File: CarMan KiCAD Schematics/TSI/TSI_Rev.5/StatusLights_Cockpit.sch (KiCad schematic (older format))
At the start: 16 parts, among them U1 RDE03110S12, U11 TLP293, U13 TLP293

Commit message: Datasheets and notes
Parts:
- D1: value Green LED -> GREEN LED; Part Name (none) -> VAOL-S8GT4
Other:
- note added: "Brake Light & RTDS\n(J18)\n"
- note added: "COCKPIT\n(J8)\n"
- note removed: "J8 COCKPIT\n"
- moved on the sheet: R15, R99, U11
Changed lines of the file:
@@
 L TSI_Rev.5-rescue:TLP293-CarMan_KiCAD_Library-TSI_Rev.5-rescue U11
 U 1 1 5F9A966C
-P 9175 3700
-F 0 "U11" H 9175 3900 50  0000 C CNN
-F 1 "TLP293" H 9175 3500 50  0000 C CNN
-F 2 "Package_SO:SOIC-4_4.55x2.6mm_P1.27mm" H 8975 3500 50  0001 L CIN
-F 3 "" H 9175 3700 50  0001 L CNN
-	1    9175 3700
+P 8875 3550
+F 0 "U11" H 8875 3750 50  0000 C CNN
+F 1 "TLP293" H 8875 3350 50  0000 C CNN
+F 2 "Package_SO:SOIC-4_4.55x2.6mm_P1.27mm" H 8675 3350 50  0001 L CIN
+F 3 "https://www.mouser.com/datasheet/2/408/Toshiba_TLP293_datasheet-1209449.pdf" H 8875 3550 50  0001 L CNN
+	1    8875 3550
 	1    0    0    -1
 $EndComp
@@
 L Device:R R15
 U 1 1 5F9DEF51
-P 8525 3600
-F 0 "R15" V 8425 3600 50  0000 C CNN
-F 1 "300" V 8525 3600 50  0000 C CNN
-F 2 "Resistor_SMD:R_0805_2012Metric_Pad1.15x1.40mm_HandSolder" V 8455 3600 50  0001 C CNN
-F 3 "~" H 8525 3600 50  0001 C CNN
-	1    8525 3600
+P 8225 3450
+F 0 "R15" V 8125 3450 50  0000 C CNN
+F 1 "300" V 8225 3450 50  0000 C CNN
+F 2 "Resistor_SMD:R_0805_2012Metric_Pad1.15x1.40mm_HandSolder" V 8155 3450 50  0001 C CNN
+F 3 "~" H 8225 3450 50  0001 C CNN
+	1    8225 3450
 	0    1    1    0
 $EndComp
-Text Label 10025 3600 2    50   ~ 0
+Text Label 9725 3450 2    50   ~ 0
 24V
-Text Label 10025 3800 2    50   ~ 0
+Text Label 9725 3650 2    50   ~ 0
 Drive_LED
-Text Label 7675 3600 0    50   ~ 0
+Text Label 7375 3450 0    50   ~ 0
 D_LED_CTRL
 Text Label 3875 3900 2    50   ~ 0
@@
 Drive_BTN
 Wire Wire Line
-	8875 3600 8675 3600
+	8575 3450 8375 3450
 Text Notes 7100 6950 0    177  ~ 0
 STATUS LIGHTS, TSAL & RTDS
@@
 F 1 "TLP293" H 2750 4234 50  0000 C CNN
 F 2 "Package_SO:SOIC-4_4.55x2.6mm_P1.27mm" H 2550 3800 50  0001 L CIN
-F 3 "" H 2750 4000 50  0001 L CNN
+F 3 "https://www.mouser.com/datasheet/2/408/Toshiba_TLP293_datasheet-1209449.pdf" H 2750 4000 50  0001 L CNN
 	1    2750 4000
 	1    0    0    -1
@@
 	4400 7000 5000 7000
 Wire Wire Line
-	7675 3600 8375 3600
-Wire Wire Line
-	7675 3800 8875 3800
-Wire Wire Line
-	9475 3600 10025 3600
-Wire Wire Line
-	9475 3800 9550 3800
+	7375 3450 8075 3450
+Wire Wire Line
+	7375 3650 8575 3650
+Wire Wire Line
+	9175 3450 9725 3450
+Wire Wire Line
+	9175 3650 9250 3650
 Wire Notes Line
 	500  2250 2250 2250
@@
 Wire Notes Line
 	500  500  500  2250
-Text Label 7675 3800 0    50   ~ 0
+Text Label 7375 3650 0    50   ~ 0
 5V_ISO_RTN
 $Comp
@@
 Wire Notes Line
 	9350 5850 9350 5500
-Text Notes 9800 5700 2    50   ~ 0
-J8 COCKPIT\n
+Text Notes 9375 5750 0    50   ~ 0
+COCKPIT\n(J8)\n
 Wire Wire Line
 	8600 5350 8900 5350
@@
 L Device:R R?
 U 1 1 605792C2
-P 9550 3950
+P 9250 3800
 AR Path="/5FE1DE7D/605792C2" Ref="R?"  Part="1"
 AR Path="/5FE1DCBA/605792C2" Ref="R99"  Part="1"
-F 0 "R99" V 9450 3950 50  0000 C CNN
-F 1 "1K" V 9550 3950 50  0000 C CNN
-F 2 "Resistor_SMD:R_0805_2012Metric_Pad1.15x1.40mm_HandSolder" V 9480 3950 50  0001 C CNN
-F 3 "~" H 9550 3950 50  0001 C CNN
-	1    9550 3950
-	1    0    0    -1
-$EndComp
-Text Label 9550 4200 0    50   ~ 0
-GLV_RTN
-Wire Wire Line
-	9550 4100 9550 4200
-Connection ~ 9550 3800
-Wire Wire Line
-	9550 3800 10025 3800
+F 0 "R99" V 9150 3800 50  0000 C CNN
+F 1 "1K" V 9250 3800 50  0000 C CNN
+F 2 "Resistor_SMD:R_0805_2012Metric_Pad1.15x1.40mm_HandSolder" V 9180 3800 50  0001 C CNN
+F 3 "~" H 9250 3800 50  0001 C CNN
+	1    9250 3800
+	1    0    0    -1
+$EndComp
+Text Label 9250 4050 0    50   ~ 0
+GLV_RTN
+Wire Wire Line
+	9250 3950 9250 4050
+Connection ~ 9250 3650
+Wire Wire Line
+	9250 3650 9725 3650
 $Comp
 L Device:LED D1
@@
 P 10200 1800
 F 0 "D1" V 10239 1682 50  0000 R CNN
-F 1 "Green LED" V 10148 1682 50  0000 R CNN
+F 1 "GREEN LED" V 10148 1682 50  0000 R CNN
 F 2 "LED_SMD:LED_0805_2012Metric_Pad1.15x1.40mm_HandSolder" H 10200 1800 50  0001 C CNN
-F 3 "~" H 10200 1800 50  0001 C CNN
+F 3 "http://static.vcclite.com/pdf/VAOL-S8GT4-LED-0805-green.pdf" H 10200 1800 50  0001 C CNN
+F 4 "VAOL-S8GT4" V 10200 1800 50  0001 C CNN "Part Name"
 	1    10200 1800
 	0    -1   -1   0
@@
 Wire Wire Line
 	3300 4100 4300 4100
+Text Notes 4225 4375 2    43   ~ 0
+Brake Light & RTDS\n(J18)\n
 $EndSCHEMATC

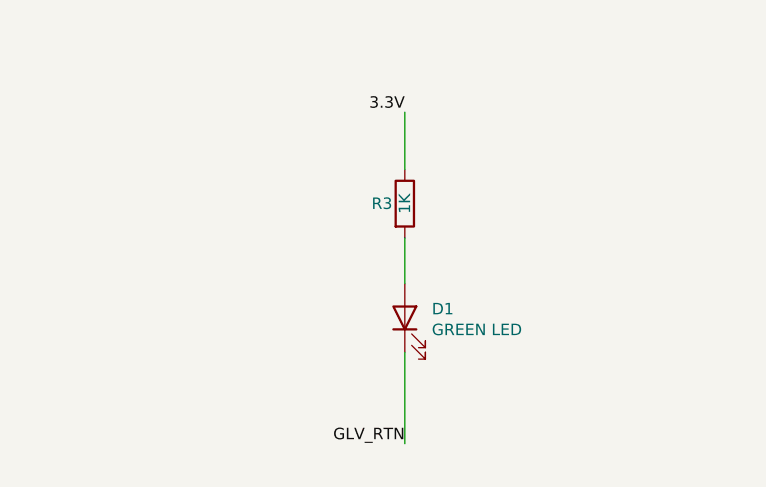
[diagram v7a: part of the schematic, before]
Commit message: Updated Resistor values for LEDs
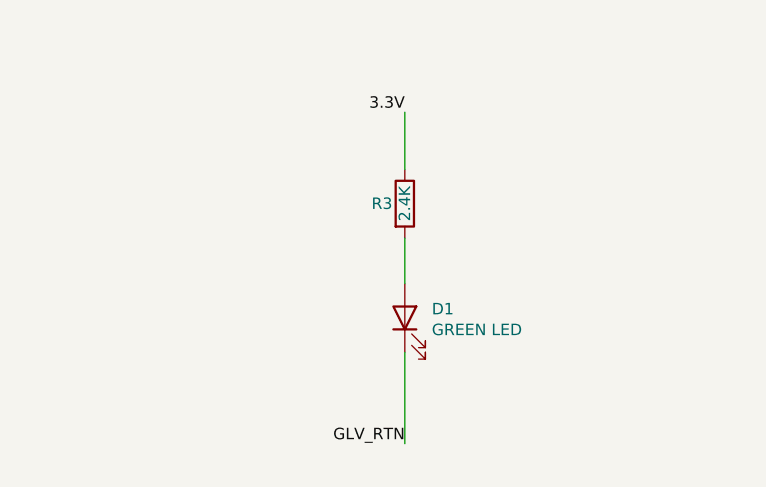
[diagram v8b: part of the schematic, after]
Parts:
- R3: value 1K -> 2.4K
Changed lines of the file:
@@
 P 10200 1300
 F 0 "R3" H 10100 1300 50  0000 C CNN
-F 1 "1K" V 10200 1300 50  0000 C CNN
+F 1 "2.4K" V 10200 1300 50  0000 C CNN
 F 2 "Resistor_SMD:R_0805_2012Metric_Pad1.15x1.40mm_HandSolder" V 10130 1300 50  0001 C CNN
 F 3 "~" H 10200 1300 50  0001 C CNN
